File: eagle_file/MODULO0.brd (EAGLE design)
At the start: 100 x 80 mm, 3 parts

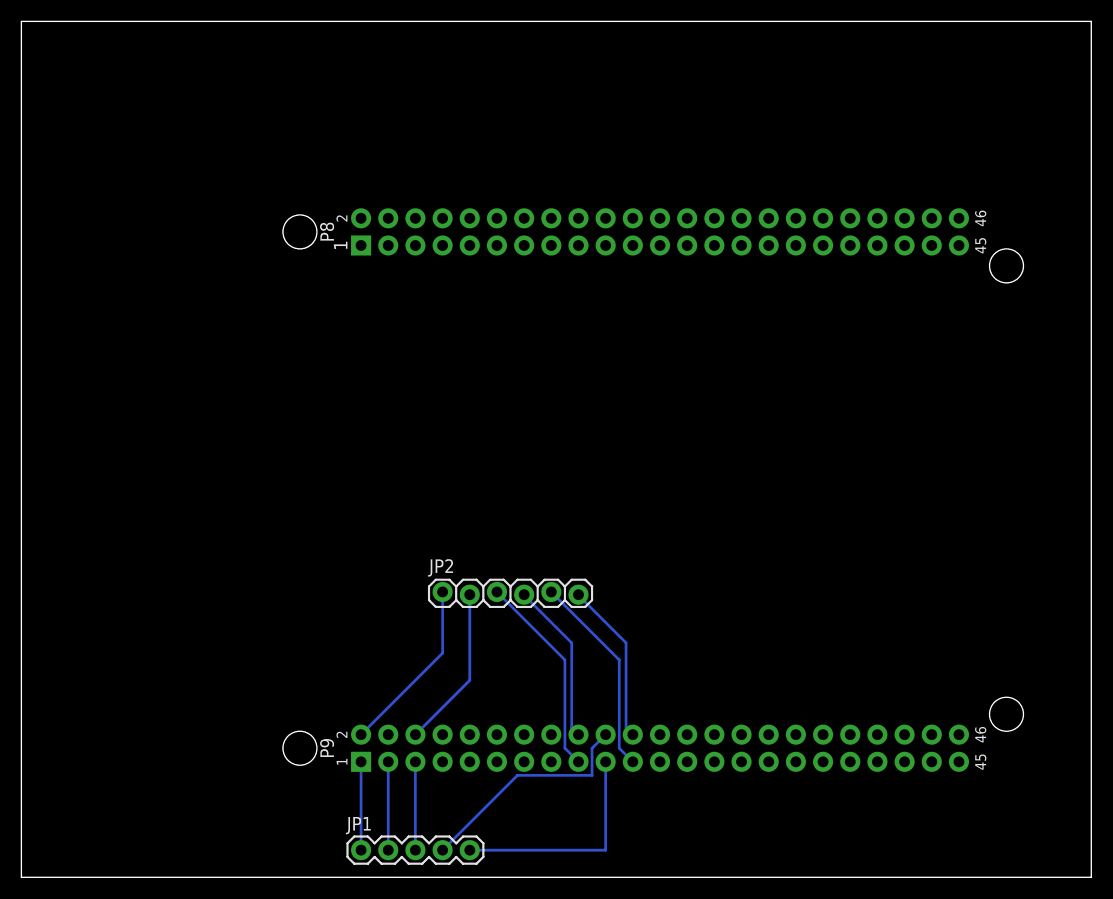
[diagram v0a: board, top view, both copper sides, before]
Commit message: GND to MODULO0
Ho messo a massa il Modulo0
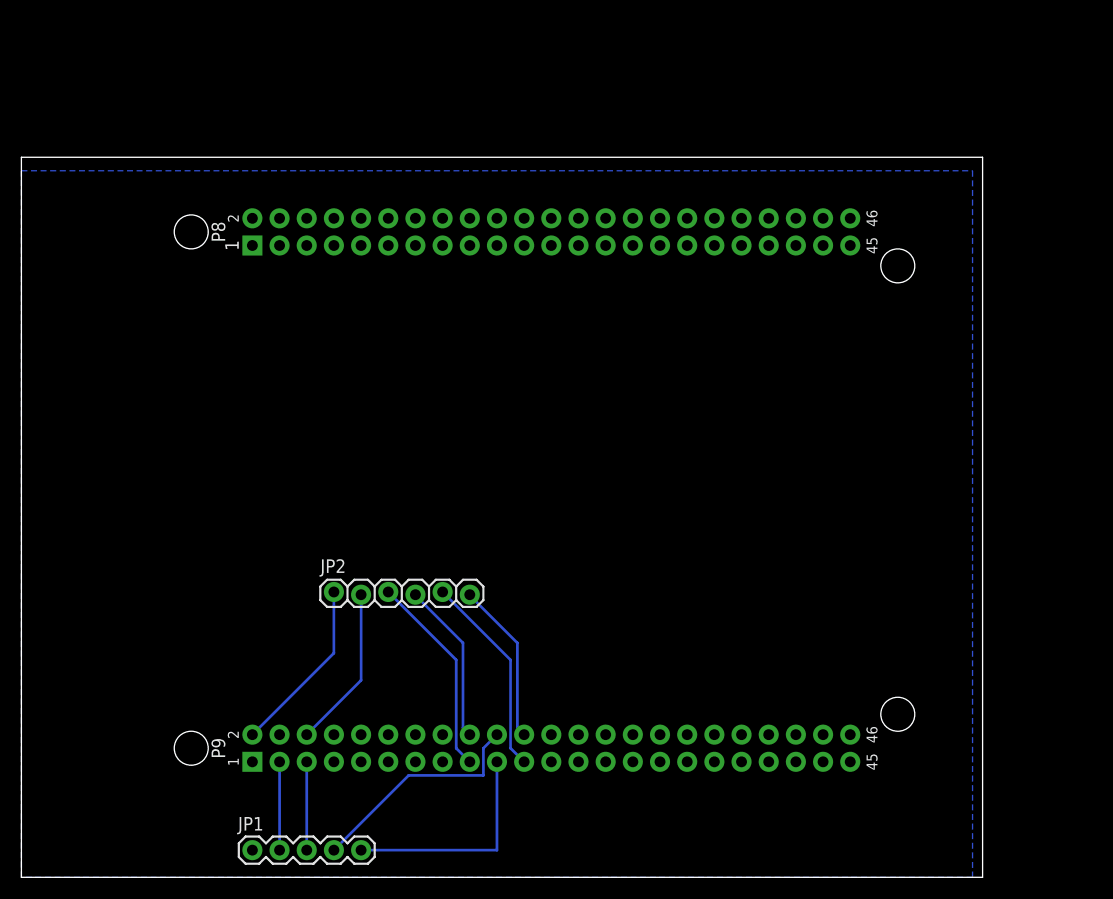
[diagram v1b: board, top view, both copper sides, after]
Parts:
- moved JP1 10.2 mm to (21.6, 2.54)
- moved U$1 10.2 mm to (1.27, 8.89)
- moved JP2 10.2 mm to (29.2, 26.7)
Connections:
- net N$1 renamed GND
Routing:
- net GND: track 8.25 -> 0.00 mm
- added copper zone on layer 16, net GND
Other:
- board size 100 x 80 mm -> 89.8 x 67.3 mm
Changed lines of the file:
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@@
 <setting verticaltext="up"/>
 </settings>
-<grid distance="0.05" unitdist="inch" unit="inch" style="lines" multiple="1" display="no" altdistance="0.025" altunitdist="inch" altunit="inch"/>
+<grid distance="0.1" unitdist="inch" unit="inch" style="lines" multiple="1" display="yes" altdistance="0.01" altunitdist="inch" altunit="inch"/>
 <layers>
 <layer number="1" name="Top" color="4" fill="1" visible="yes" active="yes"/>
@@
 <board>
 <plain>
-<wire x1="0" y1="0" x2="100" y2="0" width="0" layer="20"/>
-<wire x1="100" y1="0" x2="100" y2="80" width="0" layer="20"/>
-<wire x1="100" y1="80" x2="0" y2="80" width="0" layer="20"/>
-<wire x1="0" y1="80" x2="0" y2="0" width="0" layer="20"/>
+<wire x1="0" y1="0" x2="89.84" y2="0" width="0" layer="20"/>
+<wire x1="89.84" y1="0" x2="89.84" y2="67.3" width="0" layer="20"/>
+<wire x1="89.84" y1="67.3" x2="0" y2="67.3" width="0" layer="20"/>
+<wire x1="0" y1="67.3" x2="0" y2="0" width="0" layer="20"/>
 </plain>
 <attributes>
@@
 </autorouter>
 <elements>
-<element name="JP1" library="SparkFun-Connectors" package="1X05" value="" x="31.75" y="2.54"/>
-<element name="JP2" library="SparkFun-Connectors" package="1X06_LOCK" value="" x="39.37" y="26.67"/>
-<element name="U$1" library="SparkFun-Boards" package="BEAGLE_BONE_BLACK_CAPE" value="BEAGLE_BONE_BLACK_CAPE" x="11.43" y="8.89"/>
+<element name="JP1" library="SparkFun-Connectors" package="1X05" value="" x="21.59" y="2.54"/>
+<element name="JP2" library="SparkFun-Connectors" package="1X06_LOCK" value="" x="29.21" y="26.67"/>
+<element name="U$1" library="SparkFun-Boards" package="BEAGLE_BONE_BLACK_CAPE" value="BEAGLE_BONE_BLACK_CAPE" x="1.27" y="8.89"/>
 </elements>
 <signals>
-<signal name="N$1">
-<contactref element="JP1" pad="1"/>
-<contactref element="U$1" pad="P9.1"/>
-<wire x1="31.75" y1="10.795" x2="31.75" y2="2.54" width="0.254" layer="16"/>
-</signal>
 <signal name="N$2">
 <contactref element="JP1" pad="2"/>
 <contactref element="U$1" pad="P9.3"/>
-<wire x1="34.29" y1="10.795" x2="34.29" y2="2.54" width="0.254" layer="16"/>
+<wire x1="24.13" y1="10.795" x2="24.13" y2="2.54" width="0.254" layer="16"/>
 </signal>
 <signal name="N$3">
 <contactref element="U$1" pad="P9.5"/>
 <contactref element="JP1" pad="3"/>
-<wire x1="36.83" y1="10.795" x2="36.83" y2="2.54" width="0.254" layer="16"/>
+<wire x1="26.67" y1="10.795" x2="26.67" y2="2.54" width="0.254" layer="16"/>
 </signal>
 <signal name="N$4">
 <contactref element="U$1" pad="P9.19"/>
 <contactref element="JP1" pad="5"/>
-<wire x1="54.61" y1="2.54" x2="41.91" y2="2.54" width="0.254" layer="16"/>
-<wire x1="54.61" y1="10.795" x2="54.61" y2="2.54" width="0.254" layer="16"/>
+<wire x1="44.45" y1="2.54" x2="31.75" y2="2.54" width="0.254" layer="16"/>
+<wire x1="44.45" y1="10.795" x2="44.45" y2="2.54" width="0.254" layer="16"/>
 </signal>
 <signal name="N$5">
 <contactref element="U$1" pad="P9.20"/>
 <contactref element="JP1" pad="4"/>
-<wire x1="46.355" y1="9.525" x2="39.37" y2="2.54" width="0.254" layer="16"/>
-<wire x1="53.34" y1="9.525" x2="46.355" y2="9.525" width="0.254" layer="16"/>
-<wire x1="53.34" y1="12.065" x2="53.34" y2="9.525" width="0.254" layer="16"/>
-<wire x1="54.61" y1="13.335" x2="53.34" y2="12.065" width="0.254" layer="16"/>
+<wire x1="36.195" y1="9.525" x2="29.21" y2="2.54" width="0.254" layer="16"/>
+<wire x1="43.18" y1="9.525" x2="36.195" y2="9.525" width="0.254" layer="16"/>
+<wire x1="43.18" y1="12.065" x2="43.18" y2="9.525" width="0.254" layer="16"/>
+<wire x1="44.45" y1="13.335" x2="43.18" y2="12.065" width="0.254" layer="16"/>
 </signal>
 <signal name="N$6">
 <contactref element="JP2" pad="1"/>
 <contactref element="U$1" pad="P9.2"/>
-<wire x1="39.37" y1="20.955" x2="31.75" y2="13.335" width="0.254" layer="16"/>
-<wire x1="39.37" y1="26.67" x2="39.37" y2="20.955" width="0.254" layer="16"/>
+<wire x1="29.21" y1="20.955" x2="21.59" y2="13.335" width="0.254" layer="16"/>
+<wire x1="29.21" y1="26.67" x2="29.21" y2="20.955" width="0.254" layer="16"/>
 </signal>
 <signal name="N$7">
 <contactref element="U$1" pad="P9.6"/>
 <contactref element="JP2" pad="2"/>
-<wire x1="41.91" y1="18.415" x2="36.83" y2="13.335" width="0.254" layer="16"/>
-<wire x1="41.91" y1="26.416" x2="41.91" y2="18.415" width="0.254" layer="16"/>
+<wire x1="31.75" y1="18.415" x2="26.67" y2="13.335" width="0.254" layer="16"/>
+<wire x1="31.75" y1="26.416" x2="31.75" y2="18.415" width="0.254" layer="16"/>
 </signal>
 <signal name="N$8">
 <contactref element="U$1" pad="P9.17"/>
 <contactref element="JP2" pad="3"/>
-<wire x1="50.8" y1="12.065" x2="52.07" y2="10.795" width="0.254" layer="16"/>
-<wire x1="50.8" y1="20.32" x2="50.8" y2="12.065" width="0.254" layer="16"/>
-<wire x1="44.45" y1="26.67" x2="50.8" y2="20.32" width="0.254" layer="16"/>
+<wire x1="40.64" y1="12.065" x2="41.91" y2="10.795" width="0.254" layer="16"/>
+<wire x1="40.64" y1="20.32" x2="40.64" y2="12.065" width="0.254" layer="16"/>
+<wire x1="34.29" y1="26.67" x2="40.64" y2="20.32" width="0.254" layer="16"/>
 </signal>
 <signal name="N$9">
 <contactref element="JP2" pad="4"/>
 <contactref element="U$1" pad="P9.18"/>
-<wire x1="51.435" y1="13.97" x2="52.07" y2="13.335" width="0.254" layer="16"/>
-<wire x1="51.435" y1="21.9075" x2="51.435" y2="13.97" width="0.254" layer="16"/>
-<wire x1="46.99" y1="26.3525" x2="51.435" y2="21.9075" width="0.254" layer="16"/>
-<wire x1="46.99" y1="26.3525" x2="46.99" y2="26.416" width="0.254" layer="16"/>
+<wire x1="41.275" y1="13.97" x2="41.91" y2="13.335" width="0.254" layer="16"/>
+<wire x1="41.275" y1="21.9075" x2="41.275" y2="13.97" width="0.254" layer="16"/>
+<wire x1="36.83" y1="26.3525" x2="41.275" y2="21.9075" width="0.254" layer="16"/>
+<wire x1="36.83" y1="26.3525" x2="36.83" y2="26.416" width="0.254" layer="16"/>
 </signal>
 <signal name="N$10">
 <contactref element="U$1" pad="P9.22"/>
 <contactref element="JP2" pad="6"/>
-<wire x1="56.515" y1="13.97" x2="57.15" y2="13.335" width="0.254" layer="16"/>
-<wire x1="56.515" y1="21.9075" x2="56.515" y2="13.97" width="0.254" layer="16"/>
-<wire x1="52.07" y1="26.3525" x2="56.515" y2="21.9075" width="0.254" layer="16"/>
-<wire x1="52.07" y1="26.3525" x2="52.07" y2="26.416" width="0.254" layer="16"/>
+<wire x1="46.355" y1="13.97" x2="46.99" y2="13.335" width="0.254" layer="16"/>
+<wire x1="46.355" y1="21.9075" x2="46.355" y2="13.97" width="0.254" layer="16"/>
+<wire x1="41.91" y1="26.3525" x2="46.355" y2="21.9075" width="0.254" layer="16"/>
+<wire x1="41.91" y1="26.3525" x2="41.91" y2="26.416" width="0.254" layer="16"/>
 </signal>
 <signal name="N$11">
 <contactref element="U$1" pad="P9.21"/>
 <contactref element="JP2" pad="5"/>
-<wire x1="55.88" y1="12.065" x2="57.15" y2="10.795" width="0.254" layer="16"/>
-<wire x1="55.88" y1="20.32" x2="55.88" y2="12.065" width="0.254" layer="16"/>
-<wire x1="49.53" y1="26.67" x2="55.88" y2="20.32" width="0.254" layer="16"/>
+<wire x1="45.72" y1="12.065" x2="46.99" y2="10.795" width="0.254" layer="16"/>
+<wire x1="45.72" y1="20.32" x2="45.72" y2="12.065" width="0.254" layer="16"/>
+<wire x1="39.37" y1="26.67" x2="45.72" y2="20.32" width="0.254" layer="16"/>
+</signal>
+<signal name="GND">
+<polygon width="0.254" layer="16" isolate="0.3048">
+<vertex x="0" y="66.04"/>
+<vertex x="88.9" y="66.04"/>
+<vertex x="88.9" y="0"/>
+<vertex x="0" y="0"/>
+</polygon>
+<contactref element="JP1" pad="1"/>
+<contactref element="U$1" pad="P9.1"/>
 </signal>
 </signals>

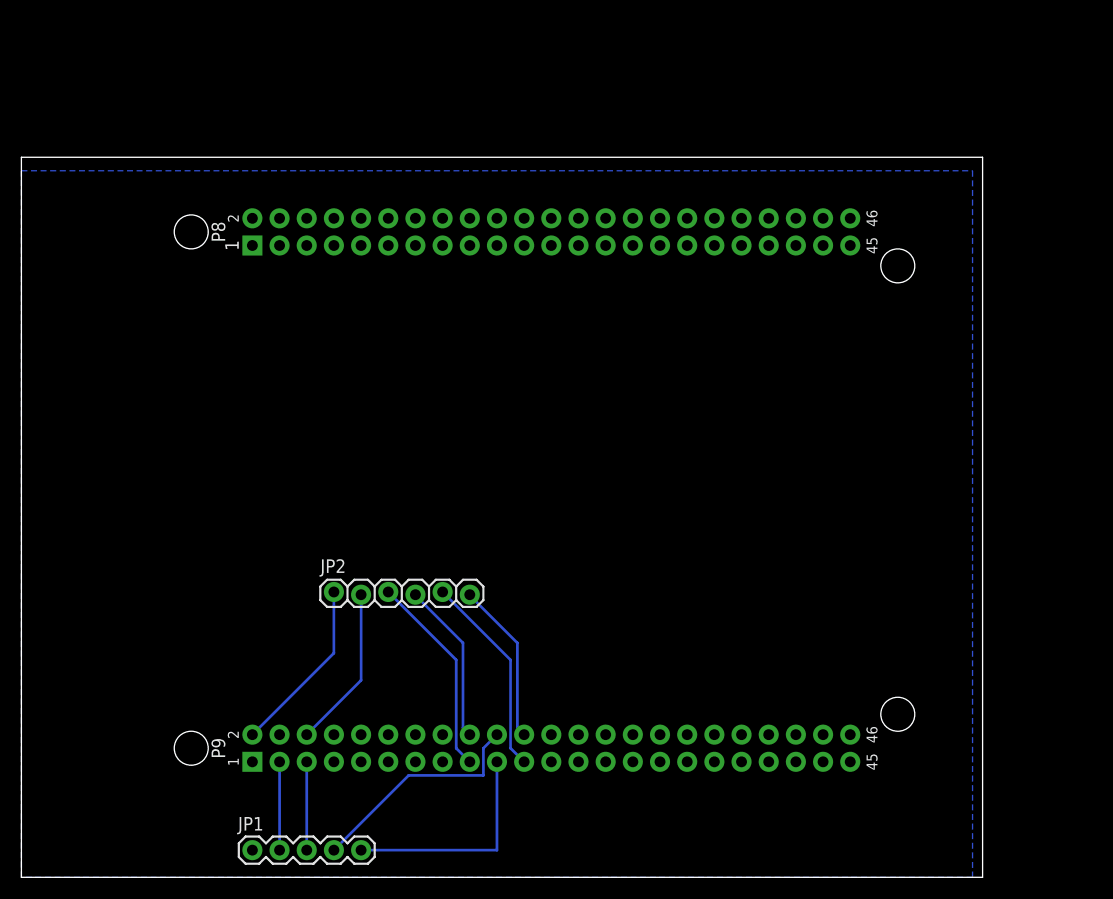
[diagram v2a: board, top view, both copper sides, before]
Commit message: Fix Modulo 0
Pin all'esterno della scheda
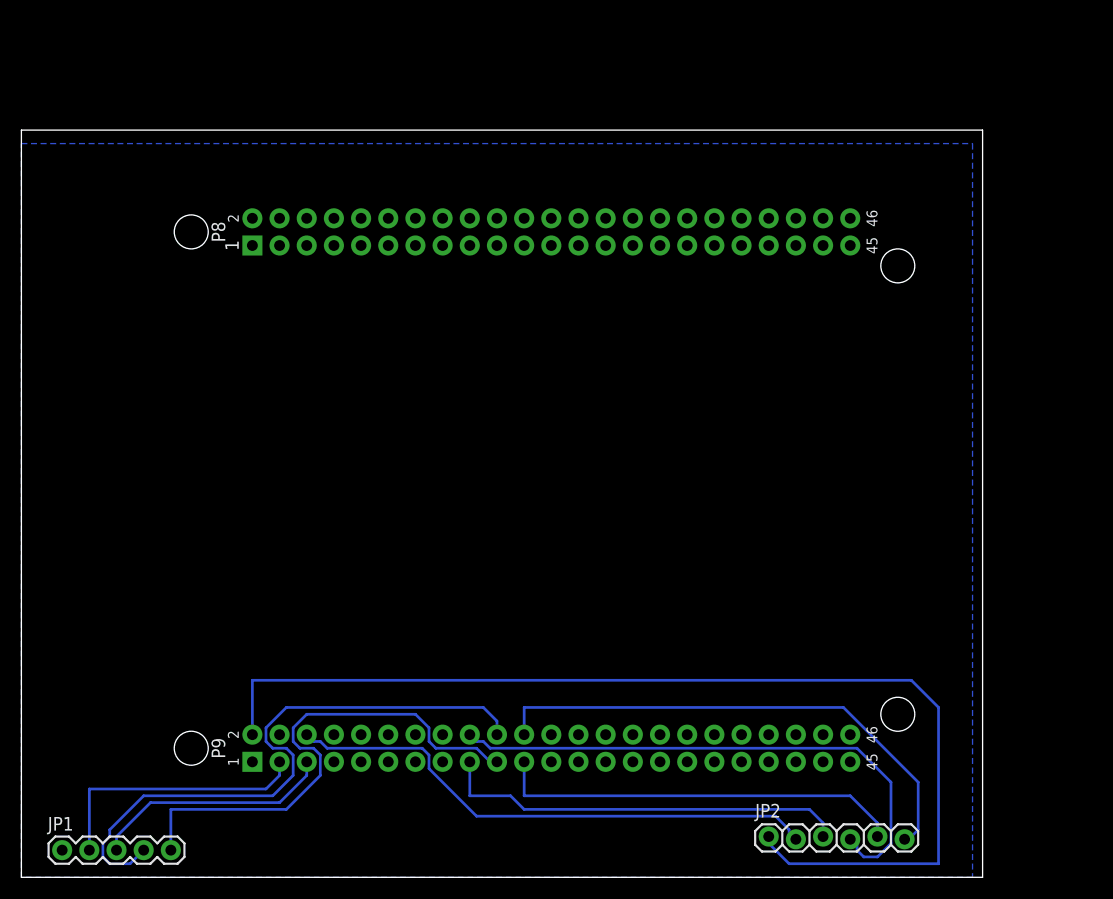
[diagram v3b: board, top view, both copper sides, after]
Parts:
- moved JP2 46.6 mm to (69.8, 3.81)
- moved JP1 17.8 mm to (3.81, 2.54)
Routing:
- net N$6: track 16.5 -> 102.2 mm
- net N$9: track 15.2 -> 52.5 mm
- net N$5: track 21.2 -> 57.1 mm
- net N$7: track 15.2 -> 51.0 mm
- net N$10: track 15.2 -> 48.5 mm
- net N$4: track 21.0 -> 47.5 mm
- net N$8: track 19.0 -> 38.5 mm
- net N$11: track 19.0 -> 38.5 mm
- net N$2: track 8.25 -> 25.3 mm
- net N$3: track 8.25 -> 22.7 mm
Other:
- board size 89.8 x 67.3 mm -> 89.8 x 69.8 mm

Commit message: Modulo1
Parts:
- JP2: device SparkFun-Connectors:1X06_LOCK -> SparkFun-Connectors:1X06
- moved U$1 12.7 mm to (-8.89, 16.5)
- moved JP1 2.54 mm to (3.81, 5.08)
- moved JP2 2.54 mm to (69.8, 6.35)
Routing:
- net N$7: track 51.0 -> 110.8 mm
- net N$9: track 52.5 -> 81.2 mm
- net N$5: track 57.1 -> 34.3 mm
- net N$4: track 47.5 -> 26.6 mm
- net N$8: track 38.5 -> 54.1 mm
- net N$11: track 38.5 -> 51.1 mm
- net N$6: track 102.2 -> 90.5 mm
- net N$10: track 48.5 -> 57.8 mm
- net N$2: track 25.3 -> 20.2 mm
- net N$3: track 22.7 -> 19.8 mm
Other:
- board size 89.8 x 69.8 mm -> 89.8 x 73.7 mm
